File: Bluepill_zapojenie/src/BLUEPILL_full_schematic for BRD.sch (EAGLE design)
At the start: 4 parts

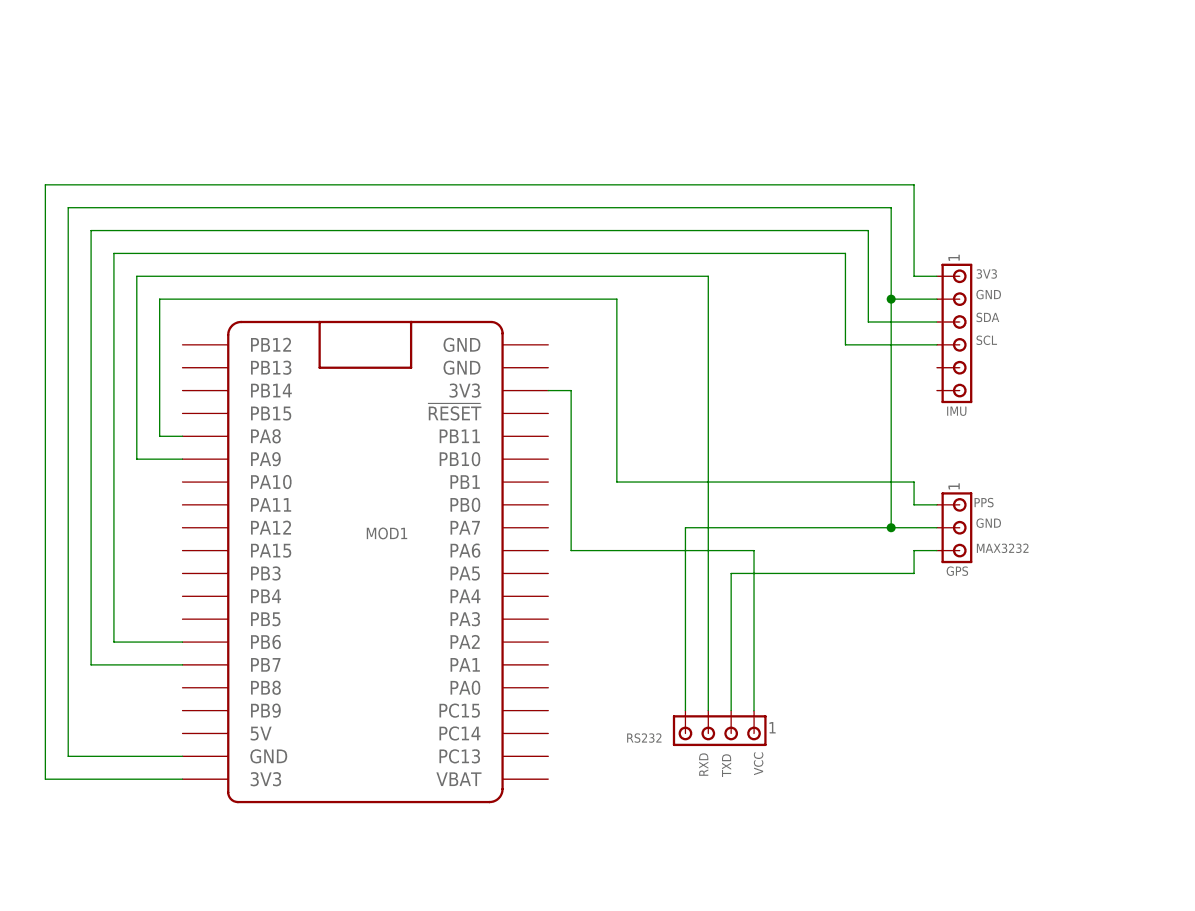
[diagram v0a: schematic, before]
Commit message: BRD schema final version
added IMU to PCB + CAM and UART connectors. 5V VCC from USB to Bluepill
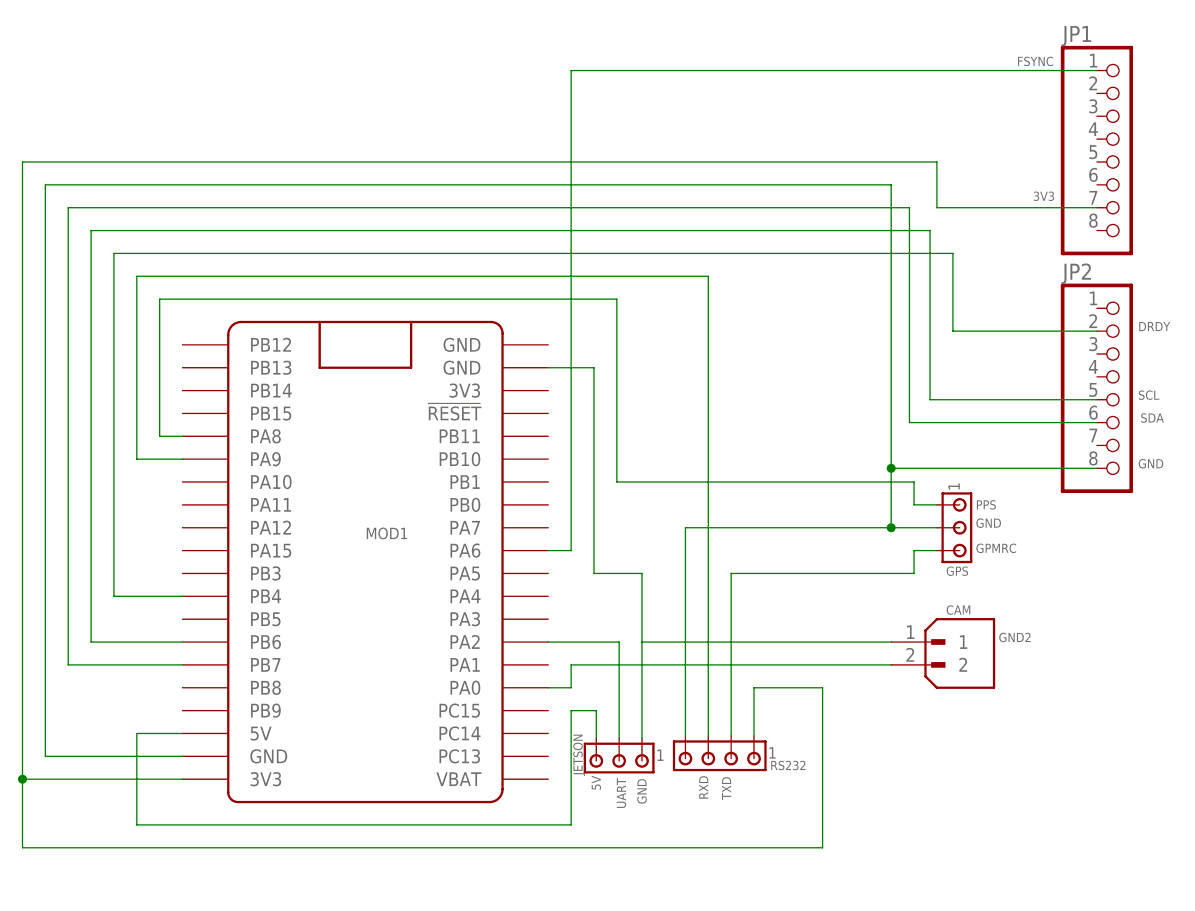
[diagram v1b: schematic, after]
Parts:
- removed IMU: (no value), con-amp:MTA06-100
- added CAM: B2B-XH-A, B2B-XH-A Model:B2B-XH-A
- added JETSON: (no value), con-amp:MTA03-100
- added JP1, JP2: (no value), pinhead:PINHD-1X8
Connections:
- net N$2 renamed PPS
- removed net VCC: MOD1.3V3@1, RS232.1
- new net 5V: JETSON.3, MOD1.5V
- new net DRDY: JP2.2, MOD1.PB4
- new net FSYNC: JP1.1, MOD1.PA6
- new net GND2: CAM.1, JETSON.1, MOD1.GND@3
- new net N$6: CAM.2, MOD1.PA0
- new net UART: JETSON.2, MOD1.PA2
- net 3V3: now also JP1.7, RS232.1; no longer IMU.1
- net GND: now also JP2.8; no longer IMU.2
- net SCL: now also JP2.5; no longer IMU.4
- net SDA: now also JP2.6; no longer IMU.3
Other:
- note added: "GPMRC"
- note added: "UART"
- note removed: "MAX3232"
- note removed: "PPS"
- moved on the sheet: RS232

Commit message: Final push
schemy, exporty final verzie
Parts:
- added 5V, 5V_STM: (no value), pinhead:PINHD-1X1
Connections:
- removed net 5V: JETSON.3, MOD1.5V
- removed net GND2: CAM.1, JETSON.1, MOD1.GND@3
- new net N$2: 5V_STM.1, MOD1.5V
- new net N$3: 5V.1, JETSON.3
- net 3V3: now also MOD1.3V3@1, RS232.4; no longer MOD1.3V3@2, RS232.1
- net GND: now also CAM.2, GPS.3, JETSON.1, RS232.1; no longer GPS.2, RS232.4
- net N$6: now also CAM.1; no longer CAM.2
- net TXD: now also GPS.2; no longer GPS.3
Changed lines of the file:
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@@
 </variantdefs>
 <classes>
-<class number="0" name="default" width="0" drill="0">
+<class number="0" name="default" width="1.016" drill="0">
 </class>
 </classes>
@@
 <part name="JP2" library="pinhead" library_urn="urn:adsk.eagle:library:325" deviceset="PINHD-1X8" device="" package3d_urn="urn:adsk.eagle:package:22409/2"/>
 <part name="JETSON" library="con-amp" library_urn="urn:adsk.eagle:library:127" deviceset="MTA03-100" device="" package3d_urn="urn:adsk.eagle:package:8081621/1"/>
+<part name="5V_STM" library="pinhead" library_urn="urn:adsk.eagle:library:325" deviceset="PINHD-1X1" device="" package3d_urn="urn:adsk.eagle:package:22485/2"/>
+<part name="5V" library="pinhead" library_urn="urn:adsk.eagle:library:325" deviceset="PINHD-1X1" device="" package3d_urn="urn:adsk.eagle:package:22485/2"/>
 </parts>
 <sheets>
 <sheet>
 <plain>
-<text x="105.918" y="55.88" size="1.016" layer="95">GND</text>
-<text x="105.918" y="53.086" size="1.016" layer="95">GPMRC</text>
+<text x="105.918" y="53.34" size="1.016" layer="95">GND</text>
+<text x="105.918" y="55.626" size="1.016" layer="95">GPMRC</text>
 <text x="69.342" y="25.146" size="1.016" layer="95" rot="R90">GND</text>
 <text x="67.056" y="24.638" size="1.016" layer="95" rot="R90">UART</text>
@@
 <attribute name="VALUE" x="61.214" y="33.782" size="1.778" layer="96" rot="R180"/>
 </instance>
+<instance part="5V_STM" gate="G$1" x="5.08" y="35.56" smashed="yes" rot="R180">
+<attribute name="NAME" x="11.43" y="32.385" size="1.778" layer="95" rot="R180"/>
+<attribute name="VALUE" x="11.43" y="40.64" size="1.778" layer="96" rot="R180"/>
+</instance>
+<instance part="5V" gate="G$1" x="60.96" y="20.32" smashed="yes" rot="R270">
+<attribute name="NAME" x="64.135" y="26.67" size="1.778" layer="95" rot="R270"/>
+<attribute name="VALUE" x="55.88" y="26.67" size="1.778" layer="96" rot="R270"/>
+</instance>
 </instances>
 <busses>
@@
 <net name="3V3" class="0">
 <segment>
-<pinref part="MOD1" gate="G$1" pin="3V3@2"/>
-<wire x1="17.78" y1="27.94" x2="0" y2="27.94" width="0.1524" layer="91"/>
-<wire x1="0" y1="27.94" x2="0" y2="96.52" width="0.1524" layer="91"/>
+<wire x1="0" y1="15.24" x2="0" y2="96.52" width="0.1524" layer="91"/>
 <wire x1="0" y1="96.52" x2="101.6" y2="96.52" width="0.1524" layer="91"/>
 <label x="112.268" y="92.202" size="1.016" layer="95"/>
-<wire x1="0" y1="27.94" x2="0" y2="20.32" width="0.1524" layer="91"/>
-<junction x="0" y="27.94"/>
-<wire x1="0" y1="20.32" x2="88.9" y2="20.32" width="0.1524" layer="91"/>
-<wire x1="88.9" y1="20.32" x2="88.9" y2="38.1" width="0.1524" layer="91"/>
-<wire x1="88.9" y1="38.1" x2="81.28" y2="38.1" width="0.1524" layer="91"/>
-<pinref part="RS232" gate="G$1" pin="1"/>
-<wire x1="81.28" y1="38.1" x2="81.28" y2="32.766" width="0.1524" layer="91"/>
+<wire x1="0" y1="15.24" x2="71.12" y2="15.24" width="0.1524" layer="91"/>
+<wire x1="101.6" y1="91.44" x2="101.6" y2="96.52" width="0.1524" layer="91"/>
+<pinref part="MOD1" gate="G$1" pin="3V3@1"/>
+<wire x1="58.42" y1="71.12" x2="109.22" y2="71.12" width="0.1524" layer="91"/>
+<wire x1="109.22" y1="71.12" x2="109.22" y2="91.44" width="0.1524" layer="91"/>
 <pinref part="JP1" gate="A" pin="7"/>
-<wire x1="119.38" y1="91.44" x2="101.6" y2="91.44" width="0.1524" layer="91"/>
-<wire x1="101.6" y1="91.44" x2="101.6" y2="96.52" width="0.1524" layer="91"/>
-</segment>
-</net>
-<net name="GND" class="0">
-<segment>
-<pinref part="MOD1" gate="G$1" pin="GND@2"/>
-<wire x1="17.78" y1="30.48" x2="2.54" y2="30.48" width="0.1524" layer="91"/>
-<wire x1="2.54" y1="30.48" x2="2.54" y2="93.98" width="0.1524" layer="91"/>
-<wire x1="2.54" y1="93.98" x2="96.52" y2="93.98" width="0.1524" layer="91"/>
-<label x="123.952" y="62.484" size="1.016" layer="95"/>
-<pinref part="GPS" gate="G$1" pin="2"/>
-<wire x1="101.6" y1="55.88" x2="96.52" y2="55.88" width="0.1524" layer="91"/>
-<wire x1="96.52" y1="55.88" x2="96.52" y2="62.484" width="0.1524" layer="91"/>
+<wire x1="109.22" y1="91.44" x2="119.38" y2="91.44" width="0.1524" layer="91"/>
+<wire x1="109.22" y1="91.44" x2="101.6" y2="91.44" width="0.1524" layer="91"/>
+<junction x="109.22" y="91.44"/>
 <pinref part="RS232" gate="G$1" pin="4"/>
-<wire x1="96.52" y1="62.484" x2="96.52" y2="93.98" width="0.1524" layer="91"/>
-<wire x1="96.52" y1="55.88" x2="73.66" y2="55.88" width="0.1524" layer="91"/>
-<wire x1="73.66" y1="55.88" x2="73.66" y2="32.766" width="0.1524" layer="91"/>
-<junction x="96.52" y="55.88"/>
-<pinref part="JP2" gate="A" pin="8"/>
-<wire x1="119.38" y1="62.484" x2="96.52" y2="62.484" width="0.1524" layer="91"/>
-<junction x="96.52" y="62.484"/>
+<wire x1="73.66" y1="32.766" x2="73.66" y2="35.56" width="0.1524" layer="91"/>
+<wire x1="73.66" y1="35.56" x2="71.12" y2="35.56" width="0.1524" layer="91"/>
+<wire x1="71.12" y1="35.56" x2="71.12" y2="15.24" width="0.1524" layer="91"/>
 </segment>
 </net>
@@
 <net name="TXD" class="0">
 <segment>
-<wire x1="99.06" y1="50.8" x2="99.06" y2="53.34" width="0.1524" layer="91"/>
 <pinref part="RS232" gate="G$1" pin="2"/>
 <wire x1="78.74" y1="32.766" x2="78.74" y2="50.8" width="0.1524" layer="91"/>
 <wire x1="78.74" y1="50.8" x2="99.06" y2="50.8" width="0.1524" layer="91"/>
 <label x="78.74" y="25.654" size="1.016" layer="95" rot="R90"/>
-<pinref part="GPS" gate="G$1" pin="3"/>
-<wire x1="101.6" y1="53.34" x2="99.06" y2="53.34" width="0.1524" layer="91"/>
+<pinref part="GPS" gate="G$1" pin="2"/>
+<wire x1="101.6" y1="55.88" x2="99.06" y2="55.88" width="0.1524" layer="91"/>
+<wire x1="99.06" y1="55.88" x2="99.06" y2="50.8" width="0.1524" layer="91"/>
 </segment>
 </net>
@@
 <net name="N$6" class="0">
 <segment>
-<pinref part="CAM" gate="G$1" pin="2"/>
-<wire x1="96.52" y1="40.64" x2="60.96" y2="40.64" width="0.1524" layer="91"/>
 <wire x1="60.96" y1="40.64" x2="60.96" y2="38.1" width="0.1524" layer="91"/>
 <pinref part="MOD1" gate="G$1" pin="PA0"/>
 <wire x1="60.96" y1="38.1" x2="58.42" y2="38.1" width="0.1524" layer="91"/>
-</segment>
-</net>
-<net name="GND2" class="0">
-<segment>
-<wire x1="68.834" y1="50.8" x2="63.5" y2="50.8" width="0.1524" layer="91"/>
-<wire x1="63.5" y1="50.8" x2="63.5" y2="73.66" width="0.1524" layer="91"/>
-<pinref part="MOD1" gate="G$1" pin="GND@3"/>
-<wire x1="63.5" y1="73.66" x2="58.42" y2="73.66" width="0.1524" layer="91"/>
-<wire x1="68.834" y1="43.18" x2="68.834" y2="50.8" width="0.1524" layer="91"/>
+<wire x1="60.96" y1="40.64" x2="91.44" y2="40.64" width="0.1524" layer="91"/>
+<wire x1="91.44" y1="40.64" x2="91.44" y2="43.18" width="0.1524" layer="91"/>
 <pinref part="CAM" gate="G$1" pin="1"/>
-<wire x1="96.52" y1="43.18" x2="68.834" y2="43.18" width="0.1524" layer="91"/>
-<wire x1="68.834" y1="43.18" x2="68.834" y2="32.512" width="0.1524" layer="91"/>
-<label x="108.458" y="43.18" size="1.016" layer="95"/>
+<wire x1="91.44" y1="43.18" x2="96.52" y2="43.18" width="0.1524" layer="91"/>
+</segment>
+</net>
+<net name="GND" class="0">
+<segment>
+<pinref part="MOD1" gate="G$1" pin="GND@2"/>
+<wire x1="17.78" y1="30.48" x2="2.54" y2="30.48" width="0.1524" layer="91"/>
+<wire x1="2.54" y1="30.48" x2="2.54" y2="93.98" width="0.1524" layer="91"/>
+<wire x1="2.54" y1="93.98" x2="96.52" y2="93.98" width="0.1524" layer="91"/>
+<label x="123.952" y="62.484" size="1.016" layer="95"/>
+<wire x1="96.52" y1="55.88" x2="96.52" y2="62.484" width="0.1524" layer="91"/>
+<wire x1="96.52" y1="62.484" x2="96.52" y2="93.98" width="0.1524" layer="91"/>
+<wire x1="96.52" y1="55.88" x2="93.98" y2="55.88" width="0.1524" layer="91"/>
+<junction x="96.52" y="55.88"/>
+<pinref part="JP2" gate="A" pin="8"/>
+<wire x1="93.98" y1="55.88" x2="81.28" y2="55.88" width="0.1524" layer="91"/>
+<wire x1="119.38" y1="62.484" x2="96.52" y2="62.484" width="0.1524" layer="91"/>
+<junction x="96.52" y="62.484"/>
+<pinref part="RS232" gate="G$1" pin="1"/>
+<wire x1="96.52" y1="53.34" x2="96.52" y2="55.88" width="0.1524" layer="91"/>
+<wire x1="81.28" y1="32.766" x2="81.28" y2="55.88" width="0.1524" layer="91"/>
+<pinref part="GPS" gate="G$1" pin="3"/>
+<wire x1="96.52" y1="53.34" x2="101.6" y2="53.34" width="0.1524" layer="91"/>
+<pinref part="CAM" gate="G$1" pin="2"/>
+<wire x1="96.52" y1="40.64" x2="93.98" y2="40.64" width="0.1524" layer="91"/>
+<wire x1="93.98" y1="40.64" x2="93.98" y2="55.88" width="0.1524" layer="91"/>
+<junction x="93.98" y="55.88"/>
 <pinref part="JETSON" gate="G$1" pin="1"/>
-</segment>
-</net>
-<net name="5V" class="0">
+<wire x1="68.834" y1="32.512" x2="68.834" y2="55.88" width="0.1524" layer="91"/>
+<wire x1="68.834" y1="55.88" x2="81.28" y2="55.88" width="0.1524" layer="91"/>
+<junction x="81.28" y="55.88"/>
+</segment>
+</net>
+<net name="N$2" class="0">
 <segment>
 <pinref part="MOD1" gate="G$1" pin="5V"/>
-<wire x1="17.78" y1="33.02" x2="12.7" y2="33.02" width="0.1524" layer="91"/>
-<wire x1="12.7" y1="33.02" x2="12.7" y2="22.86" width="0.1524" layer="91"/>
-<wire x1="12.7" y1="22.86" x2="60.96" y2="22.86" width="0.1524" layer="91"/>
+<wire x1="17.78" y1="33.02" x2="15.24" y2="33.02" width="0.1524" layer="91"/>
+<wire x1="15.24" y1="33.02" x2="15.24" y2="35.56" width="0.1524" layer="91"/>
+<pinref part="5V_STM" gate="G$1" pin="1"/>
+<wire x1="15.24" y1="35.56" x2="7.62" y2="35.56" width="0.1524" layer="91"/>
+</segment>
+</net>
+<net name="N$3" class="0">
+<segment>
+<pinref part="5V" gate="G$1" pin="1"/>
 <wire x1="60.96" y1="22.86" x2="60.96" y2="35.56" width="0.1524" layer="91"/>
 <wire x1="60.96" y1="35.56" x2="63.754" y2="35.56" width="0.1524" layer="91"/>
 <pinref part="JETSON" gate="G$1" pin="3"/>
-<wire x1="63.754" y1="32.512" x2="63.754" y2="35.56" width="0.1524" layer="91"/>
-<label x="64.262" y="26.67" size="1.016" layer="95" rot="R90"/>
-</segment>
-</net>
+<wire x1="63.754" y1="35.56" x2="63.754" y2="32.512" width="0.1524" layer="91"/>
+</segment>
+</net>
